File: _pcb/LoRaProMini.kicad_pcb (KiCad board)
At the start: 2 copper layers, 92 x 27 mm, 23 parts, among them J1 Conn_01x02, J2 Conn_01x03, J3 Conn_01x04, J4 Conn_01x04, U1 MCP1700-3302E_SOT23, U2 RFM95W-868S2, X1 Arduino_Pro_Mini

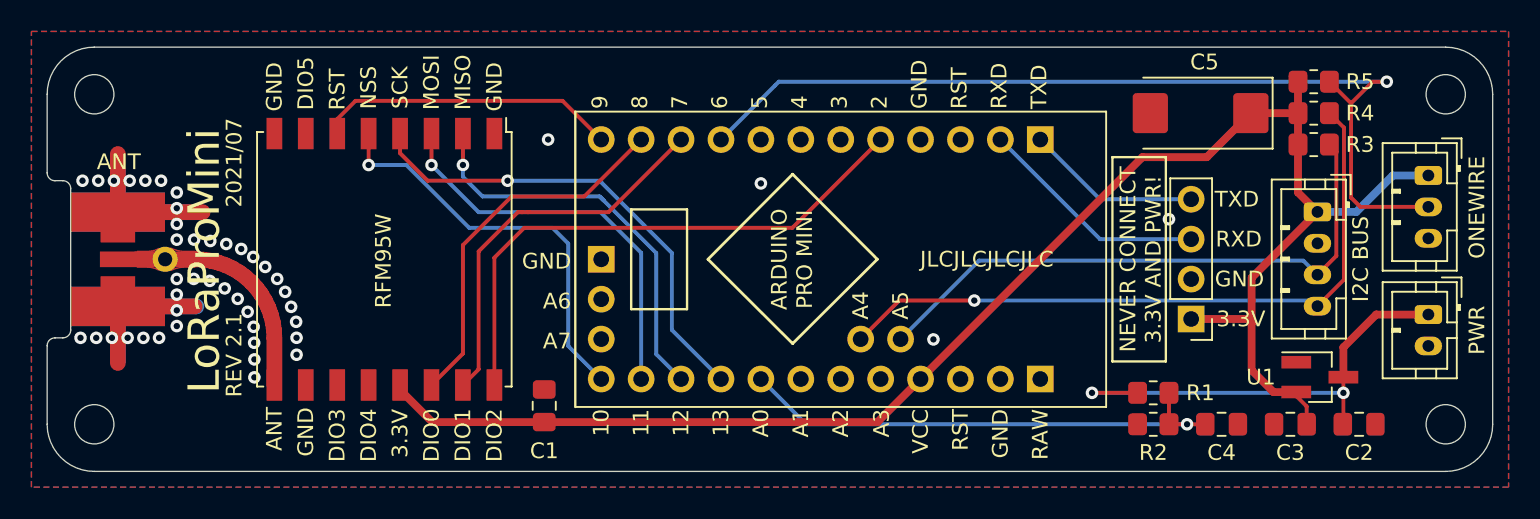
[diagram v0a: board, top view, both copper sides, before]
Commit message: Added RST Pin to Programmer Interface
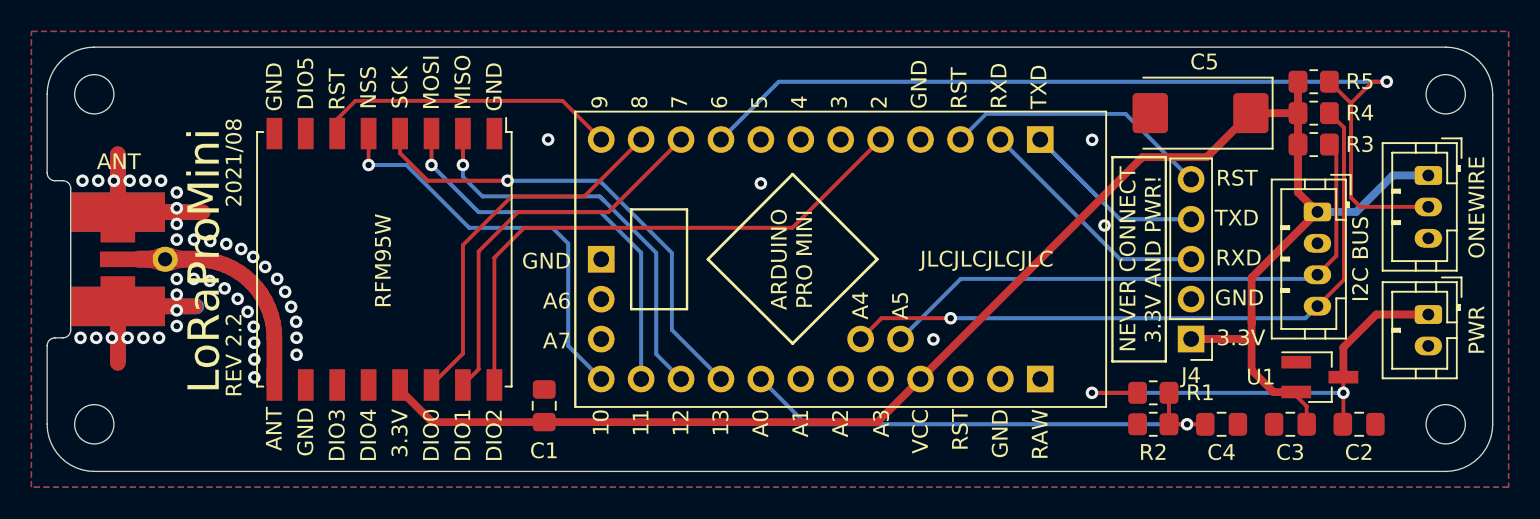
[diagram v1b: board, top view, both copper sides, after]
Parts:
- J4: value Conn_01x04 -> Conn_01x05; footprint Connector_PinHeader_2.54mm:PinHeader_1x04_P2.54mm_Vertical -> Connector_PinHeader_2.54mm:PinHeader_1x05_P2.54mm_Vertical
- moved J4 1.28 mm to (171.7, 95.8)
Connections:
- X1 pad 3: Net-(X1-Pad3) -> MCU_RST
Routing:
- net MCU_RST: track 0.00 -> 17.1 mm
- net TXD: track 10.6 -> 17.4 mm
- net RXD: track 14.2 -> 15.3 mm
- net +3V3: track 108.3 -> 107.7 mm
- net GND: vias 45 -> 46
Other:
- board text added: "2021/08"
- board text added: "REV 2.2"
- board text added: "RST"
- board text removed: "2021/07"
- board text removed: "REV 2.1"
